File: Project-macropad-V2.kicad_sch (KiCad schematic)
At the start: 47 parts

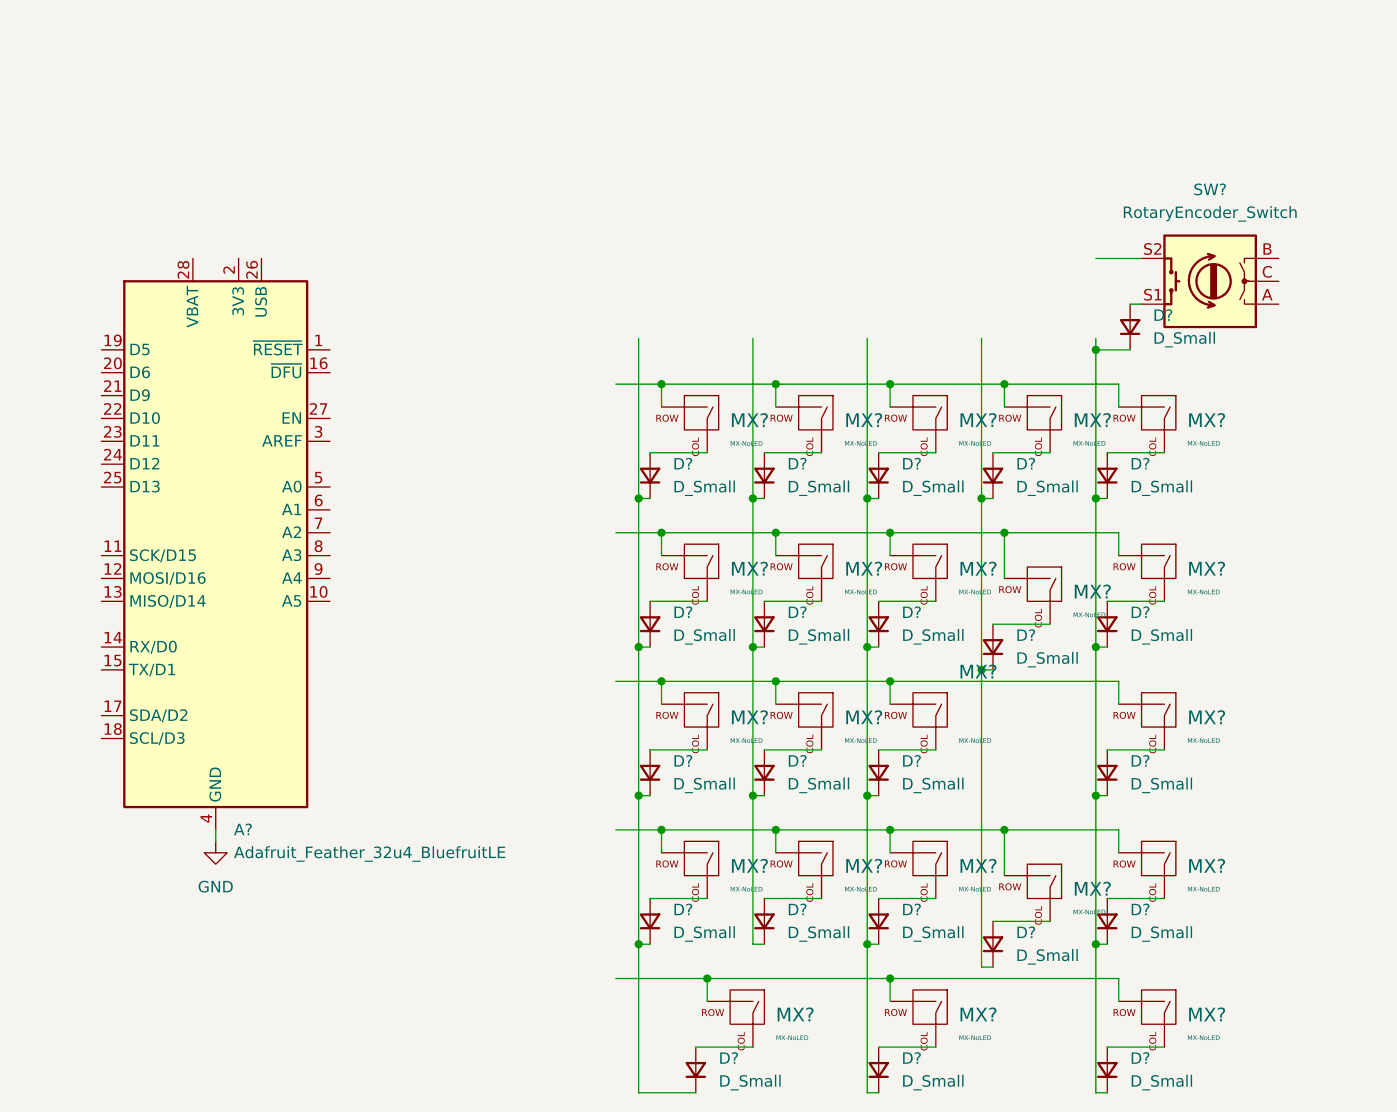
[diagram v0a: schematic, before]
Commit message: Schematic done
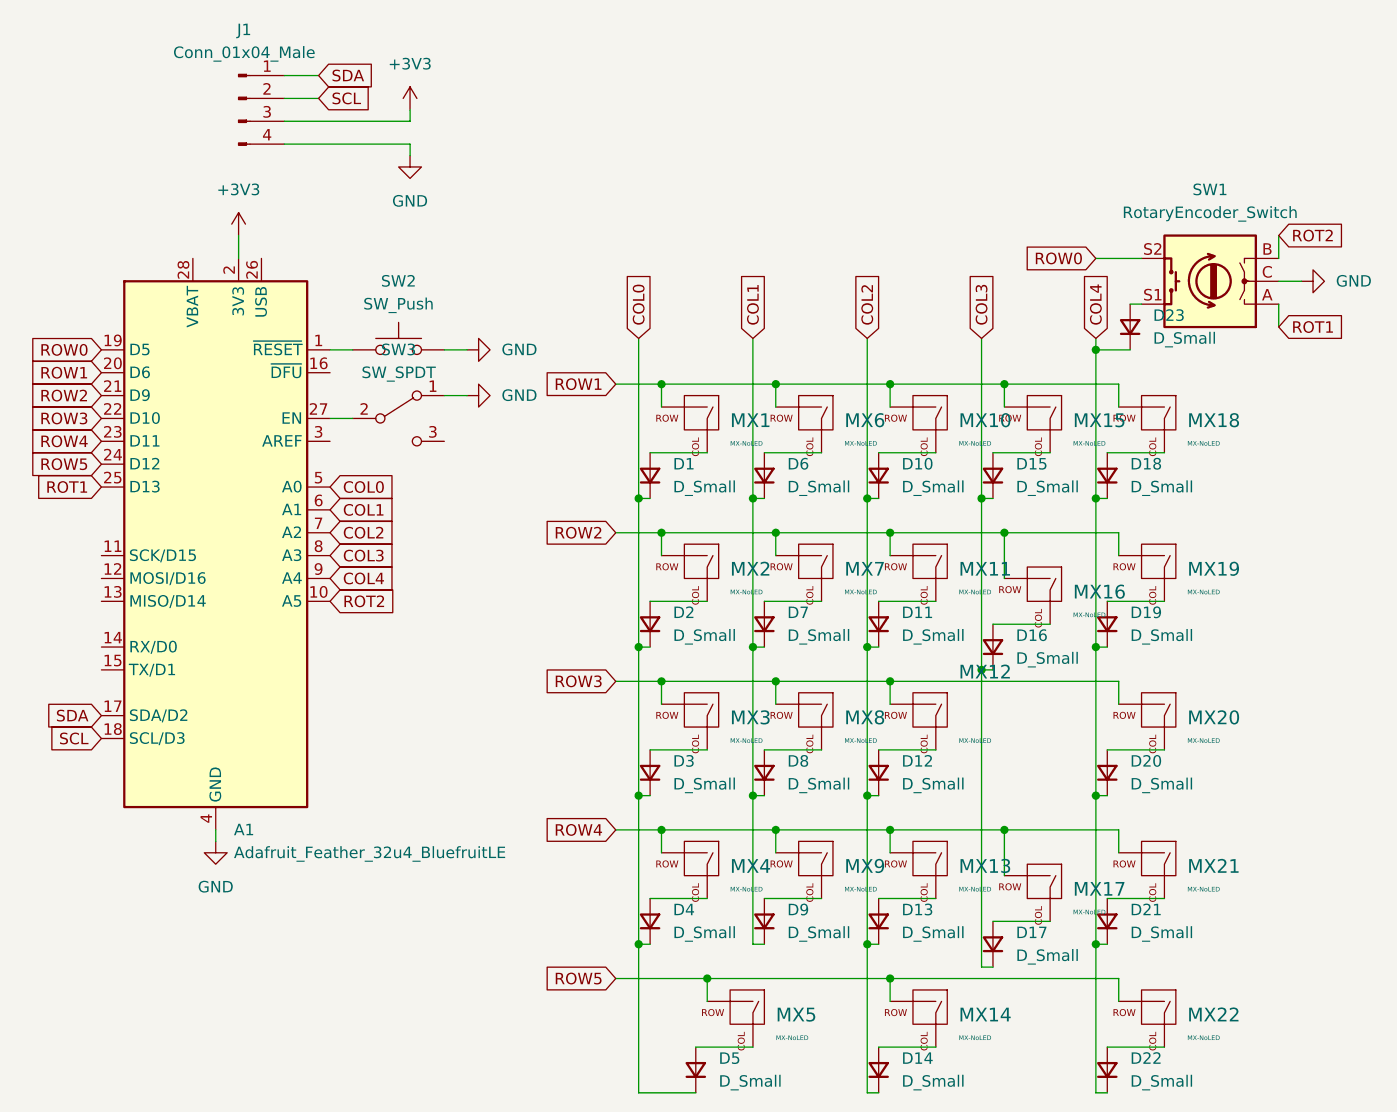
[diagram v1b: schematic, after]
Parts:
- added J1: Conn_01x04_Male, KiCad-SSD1306-0.91-OLED-4pin-128x32:SSD1306-0.91-OLED-4pin-128x32, symbol Connector:Conn_01x04_Male
- added SW2: SW_Push, random-keyboard-parts:SKQG-1155865, symbol Switch:SW_Push
- added SW3: SW_SPDT, Button_Switch_THT:SW_Slide_1P2T_CK_OS102011MS2Q, symbol Switch:SW_SPDT
- D1, D10, D11, D12, D13, D14, D15, D16, D17, D18, D19, D2, D20, D21, D22, D23, D3, D4, D5, D6, D7, D8, D9: renamed from D?; footprint (none) -> Diode_THT:D_DO-35_SOD27_P7.62mm_Horizontal
- MX1, MX10, MX11, MX12, MX13, MX14, MX15, MX18, MX19, MX2, MX20, MX21, MX22, MX3, MX4, MX6, MX7, MX8, MX9: renamed from MX?; footprint (none) -> MX_Alps_Hybrid:MX-1U-NoLED
- MX16, MX17, MX5: renamed from MX?; footprint (none) -> MX_Alps_Hybrid:MX-2U-NoLED
- SW1: renamed from SW?; footprint (none) -> Rotary_Encoder:RotaryEncoder_Alps_EC11E-Switch_Vertical_H20mm_CircularMountingHoles
- gave numbers to parts that had none: 1
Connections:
- net GND: now also SW1.C, J1.4 (Pin_4), SW2.2, SW3.1 (A)
- net ROW4: now reaches MX13.2 (ROW), MX17.2 (ROW), MX21.2 (ROW), MX4.2 (ROW), MX9.2 (ROW)
- net ROW4: now also A1.23 (D11)
- net COL4: now reaches D18.1 (K), D19.1 (K), D20.1 (K), D21.1 (K), D22.1 (K), D23.1 (K)
- net COL4: now also A1.9 (A4)
- net COL1: now reaches D6.1 (K), D7.1 (K), D8.1 (K), D9.1 (K)
- net COL1: now also A1.6 (A1)
- net COL3: now reaches D15.1 (K), D16.1 (K), D17.1 (K)
- net COL3: now also A1.8 (A3)
- net ROT1: now reaches SW1.A
- net ROT1: now also A1.25 (D13)
- net ROT2: now reaches SW1.B
- net ROT2: now also A1.10 (A5)
- net ROW0: now reaches SW1.S2
- net ROW0: now also A1.19 (D5)
- net ROW3: now reaches MX12.2 (ROW), MX20.2 (ROW), MX3.2 (ROW), MX8.2 (ROW)
- net ROW3: now also A1.22 (D10)
- net COL2: now reaches D10.1 (K), D11.1 (K), D12.1 (K), D13.1 (K), D14.1 (K)
- net COL2: now also A1.7 (A2)
- net COL0: now reaches D1.1 (K), D2.1 (K), D3.1 (K), D4.1 (K), D5.1 (K)
- net COL0: now also A1.5 (A0)
- net ROW2: now reaches MX11.2 (ROW), MX16.2 (ROW), MX19.2 (ROW), MX2.2 (ROW), MX7.2 (ROW)
- net ROW2: now also A1.21 (D9)
- net ROW1: now reaches MX1.2 (ROW), MX10.2 (ROW), MX15.2 (ROW), MX18.2 (ROW), MX6.2 (ROW)
- net ROW1: now also A1.20 (D6)
- net ROW5: now reaches MX14.2 (ROW), MX22.2 (ROW), MX5.2 (ROW)
- net ROW5: now also A1.24 (D12)
- net at A1.1 (~{RESET}): now also SW2.1
- net SDA: now reaches A1.17 (SDA/D2)
- net SDA: now also J1.1 (Pin_1)
- net SCL: now reaches A1.18 (SCL/D3)
- net SCL: now also J1.2 (Pin_2)
- net +3V3: now reaches A1.2 (3V3)
- net +3V3: now also J1.3 (Pin_3)
- net at A1.27 (EN): now also SW3.2 (B)

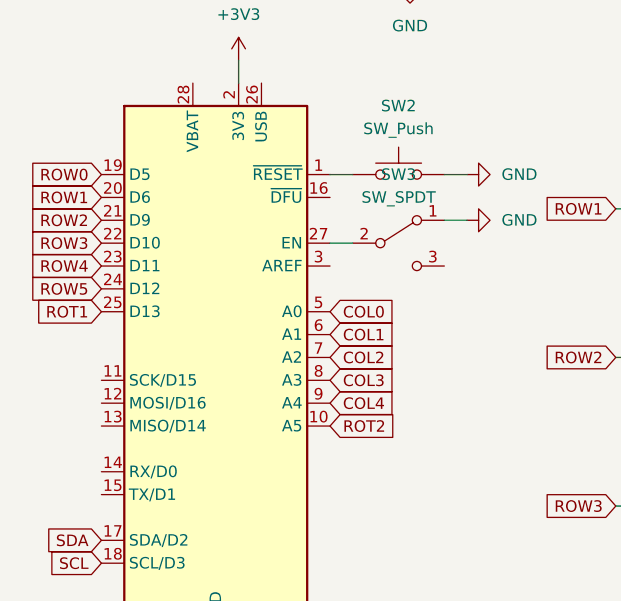
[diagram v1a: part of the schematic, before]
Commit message: PCB Routing done
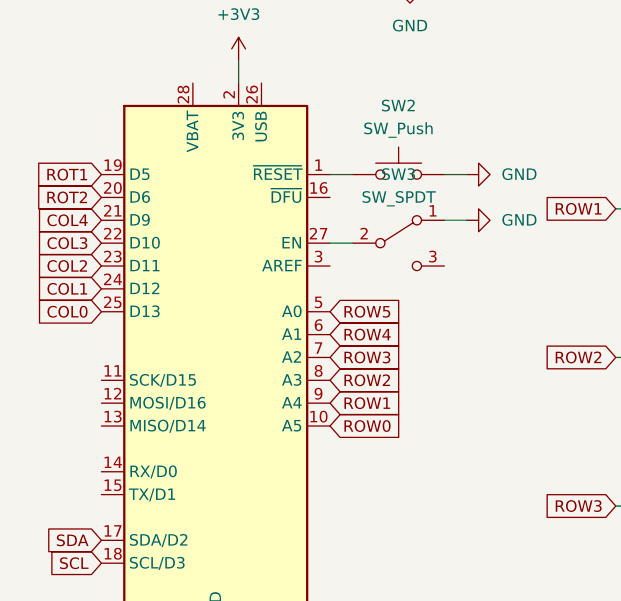
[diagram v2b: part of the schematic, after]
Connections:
- net COL0: now also A1.25 (D13); no longer A1.5 (A0)
- net COL1: now also A1.24 (D12); no longer A1.6 (A1)
- net COL2: now also A1.23 (D11); no longer A1.7 (A2)
- net COL3: now also A1.22 (D10); no longer A1.8 (A3)
- net COL4: now also A1.21 (D9); no longer A1.9 (A4)
- net ROT1: now also A1.19 (D5); no longer A1.25 (D13)
- net ROT2: now also A1.20 (D6); no longer A1.10 (A5)
- net ROW0: now also A1.10 (A5); no longer A1.19 (D5)
- net ROW1: now also A1.9 (A4); no longer A1.20 (D6)
- net ROW2: now also A1.8 (A3); no longer A1.21 (D9)
- net ROW3: now also A1.7 (A2); no longer A1.22 (D10)
- net ROW4: now also A1.6 (A1); no longer A1.23 (D11)
- net ROW5: now also A1.5 (A0); no longer A1.24 (D12)
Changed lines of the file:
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@@
     )
   )
-  (global_label "ROT1" (shape input) (at 48.26 71.12 180) (fields_autoplaced)
-    (effects (font (size 1.27 1.27)) (justify right))
-    (property "Intersheet References" "${INTERSHEET_REFS}" (id 0) (at 41.0693 71.0406 0)
-      (effects (font (size 1.27 1.27)) (justify right) hide)
-    )
-  )
-  (global_label "ROW4" (shape input) (at 48.26 66.04 180) (fields_autoplaced)
-    (effects (font (size 1.27 1.27)) (justify right))
-    (property "Intersheet References" "${INTERSHEET_REFS}" (id 0) (at 40.5855 65.9606 0)
-      (effects (font (size 1.27 1.27)) (justify right) hide)
+  (global_label "ROT1" (shape input) (at 48.26 55.88 180) (fields_autoplaced)
+    (effects (font (size 1.27 1.27)) (justify right))
+    (property "Intersheet References" "${INTERSHEET_REFS}" (id 0) (at 41.0693 55.8006 0)
+      (effects (font (size 1.27 1.27)) (justify right) hide)
+    )
+  )
+  (global_label "ROW4" (shape input) (at 73.66 73.66 0) (fields_autoplaced)
+    (effects (font (size 1.27 1.27)) (justify left))
+    (property "Intersheet References" "${INTERSHEET_REFS}" (id 0) (at 81.3345 73.7394 0)
+      (effects (font (size 1.27 1.27)) (justify left) hide)
     )
   )
@@
     )
   )
-  (global_label "COL3" (shape input) (at 73.66 78.74 0) (fields_autoplaced)
-    (effects (font (size 1.27 1.27)) (justify left))
-    (property "Intersheet References" "${INTERSHEET_REFS}" (id 0) (at 80.9112 78.6606 0)
-      (effects (font (size 1.27 1.27)) (justify left) hide)
+  (global_label "COL3" (shape input) (at 48.26 63.5 180) (fields_autoplaced)
+    (effects (font (size 1.27 1.27)) (justify right))
+    (property "Intersheet References" "${INTERSHEET_REFS}" (id 0) (at 41.0088 63.5794 0)
+      (effects (font (size 1.27 1.27)) (justify right) hide)
     )
   )
@@
     )
   )
-  (global_label "COL1" (shape input) (at 73.66 73.66 0) (fields_autoplaced)
-    (effects (font (size 1.27 1.27)) (justify left))
-    (property "Intersheet References" "${INTERSHEET_REFS}" (id 0) (at 80.9112 73.5806 0)
-      (effects (font (size 1.27 1.27)) (justify left) hide)
+  (global_label "COL1" (shape input) (at 48.26 68.58 180) (fields_autoplaced)
+    (effects (font (size 1.27 1.27)) (justify right))
+    (property "Intersheet References" "${INTERSHEET_REFS}" (id 0) (at 41.0088 68.6594 0)
+      (effects (font (size 1.27 1.27)) (justify right) hide)
     )
   )
@@
     )
   )
-  (global_label "ROT2" (shape input) (at 73.66 83.82 0) (fields_autoplaced)
-    (effects (font (size 1.27 1.27)) (justify left))
-    (property "Intersheet References" "${INTERSHEET_REFS}" (id 0) (at 80.8507 83.7406 0)
-      (effects (font (size 1.27 1.27)) (justify left) hide)
+  (global_label "ROT2" (shape input) (at 48.26 58.42 180) (fields_autoplaced)
+    (effects (font (size 1.27 1.27)) (justify right))
+    (property "Intersheet References" "${INTERSHEET_REFS}" (id 0) (at 41.0693 58.4994 0)
+      (effects (font (size 1.27 1.27)) (justify right) hide)
     )
   )
@@
     )
   )
-  (global_label "ROW3" (shape input) (at 48.26 63.5 180) (fields_autoplaced)
-    (effects (font (size 1.27 1.27)) (justify right))
-    (property "Intersheet References" "${INTERSHEET_REFS}" (id 0) (at 40.5855 63.4206 0)
-      (effects (font (size 1.27 1.27)) (justify right) hide)
+  (global_label "ROW3" (shape input) (at 73.66 76.2 0) (fields_autoplaced)
+    (effects (font (size 1.27 1.27)) (justify left))
+    (property "Intersheet References" "${INTERSHEET_REFS}" (id 0) (at 81.3345 76.2794 0)
+      (effects (font (size 1.27 1.27)) (justify left) hide)
     )
   )
@@
     )
   )
-  (global_label "ROW2" (shape input) (at 48.26 60.96 180) (fields_autoplaced)
-    (effects (font (size 1.27 1.27)) (justify right))
-    (property "Intersheet References" "${INTERSHEET_REFS}" (id 0) (at 40.5855 60.8806 0)
-      (effects (font (size 1.27 1.27)) (justify right) hide)
-    )
-  )
-  (global_label "COL0" (shape input) (at 73.66 71.12 0) (fields_autoplaced)
-    (effects (font (size 1.27 1.27)) (justify left))
-    (property "Intersheet References" "${INTERSHEET_REFS}" (id 0) (at 80.9112 71.0406 0)
-      (effects (font (size 1.27 1.27)) (justify left) hide)
-    )
-  )
-  (global_label "COL4" (shape input) (at 73.66 81.28 0) (fields_autoplaced)
-    (effects (font (size 1.27 1.27)) (justify left))
-    (property "Intersheet References" "${INTERSHEET_REFS}" (id 0) (at 80.9112 81.2006 0)
-      (effects (font (size 1.27 1.27)) (justify left) hide)
+  (global_label "ROW2" (shape input) (at 73.66 78.74 0) (fields_autoplaced)
+    (effects (font (size 1.27 1.27)) (justify left))
+    (property "Intersheet References" "${INTERSHEET_REFS}" (id 0) (at 81.3345 78.8194 0)
+      (effects (font (size 1.27 1.27)) (justify left) hide)
+    )
+  )
+  (global_label "COL0" (shape input) (at 48.26 71.12 180) (fields_autoplaced)
+    (effects (font (size 1.27 1.27)) (justify right))
+    (property "Intersheet References" "${INTERSHEET_REFS}" (id 0) (at 41.0088 71.1994 0)
+      (effects (font (size 1.27 1.27)) (justify right) hide)
+    )
+  )
+  (global_label "COL4" (shape input) (at 48.26 60.96 180) (fields_autoplaced)
+    (effects (font (size 1.27 1.27)) (justify right))
+    (property "Intersheet References" "${INTERSHEET_REFS}" (id 0) (at 41.0088 61.0394 0)
+      (effects (font (size 1.27 1.27)) (justify right) hide)
     )
   )
@@
     )
   )
-  (global_label "ROW0" (shape input) (at 48.26 55.88 180) (fields_autoplaced)
-    (effects (font (size 1.27 1.27)) (justify right))
-    (property "Intersheet References" "${INTERSHEET_REFS}" (id 0) (at 40.5855 55.8006 0)
-      (effects (font (size 1.27 1.27)) (justify right) hide)
+  (global_label "ROW0" (shape input) (at 73.66 83.82 0) (fields_autoplaced)
+    (effects (font (size 1.27 1.27)) (justify left))
+    (property "Intersheet References" "${INTERSHEET_REFS}" (id 0) (at 81.3345 83.8994 0)
+      (effects (font (size 1.27 1.27)) (justify left) hide)
     )
   )
@@
     )
   )
-  (global_label "ROW1" (shape input) (at 48.26 58.42 180) (fields_autoplaced)
-    (effects (font (size 1.27 1.27)) (justify right))
-    (property "Intersheet References" "${INTERSHEET_REFS}" (id 0) (at 40.5855 58.3406 0)
-      (effects (font (size 1.27 1.27)) (justify right) hide)
+  (global_label "ROW1" (shape input) (at 73.66 81.28 0) (fields_autoplaced)
+    (effects (font (size 1.27 1.27)) (justify left))
+    (property "Intersheet References" "${INTERSHEET_REFS}" (id 0) (at 81.3345 81.3594 0)
+      (effects (font (size 1.27 1.27)) (justify left) hide)
     )
   )
@@
     )
   )
-  (global_label "COL2" (shape input) (at 73.66 76.2 0) (fields_autoplaced)
-    (effects (font (size 1.27 1.27)) (justify left))
-    (property "Intersheet References" "${INTERSHEET_REFS}" (id 0) (at 80.9112 76.1206 0)
-      (effects (font (size 1.27 1.27)) (justify left) hide)
-    )
-  )
-  (global_label "ROW5" (shape input) (at 48.26 68.58 180) (fields_autoplaced)
-    (effects (font (size 1.27 1.27)) (justify right))
-    (property "Intersheet References" "${INTERSHEET_REFS}" (id 0) (at 40.5855 68.5006 0)
-      (effects (font (size 1.27 1.27)) (justify right) hide)
+  (global_label "COL2" (shape input) (at 48.26 66.04 180) (fields_autoplaced)
+    (effects (font (size 1.27 1.27)) (justify right))
+    (property "Intersheet References" "${INTERSHEET_REFS}" (id 0) (at 41.0088 66.1194 0)
+      (effects (font (size 1.27 1.27)) (justify right) hide)
+    )
+  )
+  (global_label "ROW5" (shape input) (at 73.66 71.12 0) (fields_autoplaced)
+    (effects (font (size 1.27 1.27)) (justify left))
+    (property "Intersheet References" "${INTERSHEET_REFS}" (id 0) (at 81.3345 71.1994 0)
+      (effects (font (size 1.27 1.27)) (justify left) hide)
     )
   )
@@
   (symbol (lib_id "power:+3V3") (at 63.5 43.18 0) (unit 1)
     (in_bom yes) (on_board yes) (fields_autoplaced)
-    (property "Reference" "#PWR?" (id 0) (at 63.5 46.99 0)
+    (property "Reference" "#PWR0107" (id 0) (at 63.5 46.99 0)
       (effects (font (size 1.27 1.27)) hide)
     )
@@
     )
     (path "/e19e40ba-f814-43d7-b94d-88d0c42000fe"
-      (reference "#PWR?") (unit 1) (value "+3V3") (footprint "")
+      (reference "#PWR0107") (unit 1) (value "+3V3") (footprint "")
     )
     (path "/94edec88-fccc-4226-a5d3-6514e0ea7646"
